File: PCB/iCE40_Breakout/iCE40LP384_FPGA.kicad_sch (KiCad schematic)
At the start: 24 parts, among them J1 Conn_01x08, J2 Conn_01x10, J3 Conn_01x10, Q1 2N7002, SW1 KH-6X6X5H-STM, U1 ICE40LP384-SG32

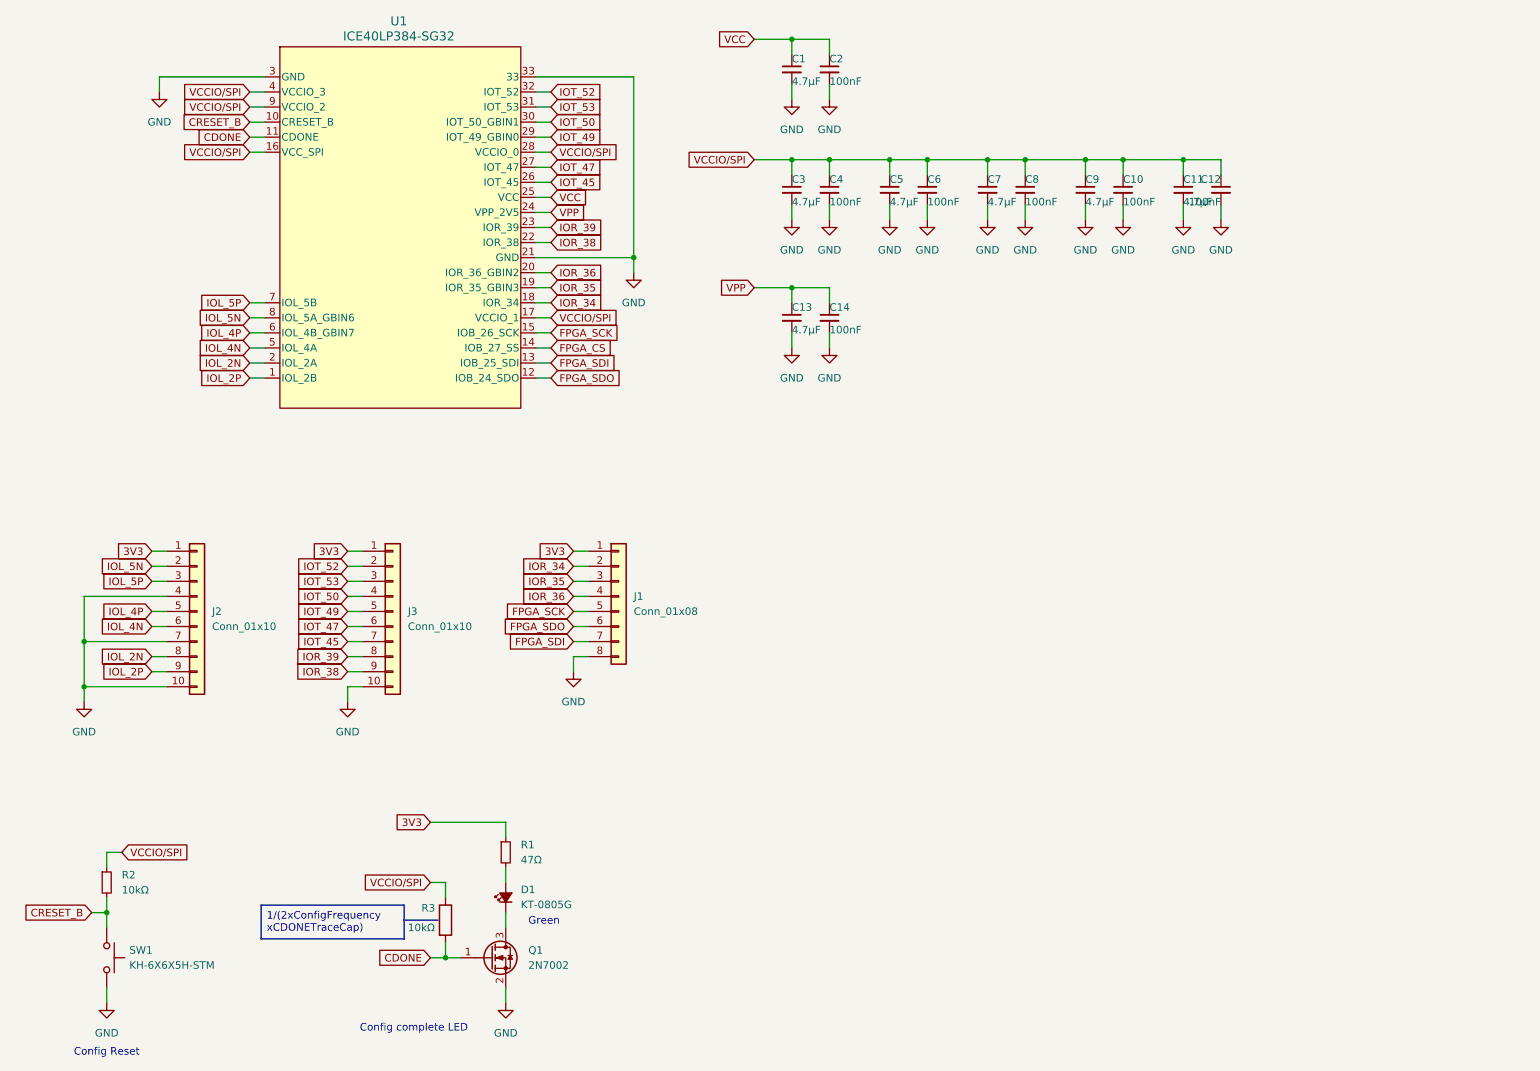
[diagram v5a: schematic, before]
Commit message: Changed all manually placed components into DNP, and changed the manually added caps to 0603
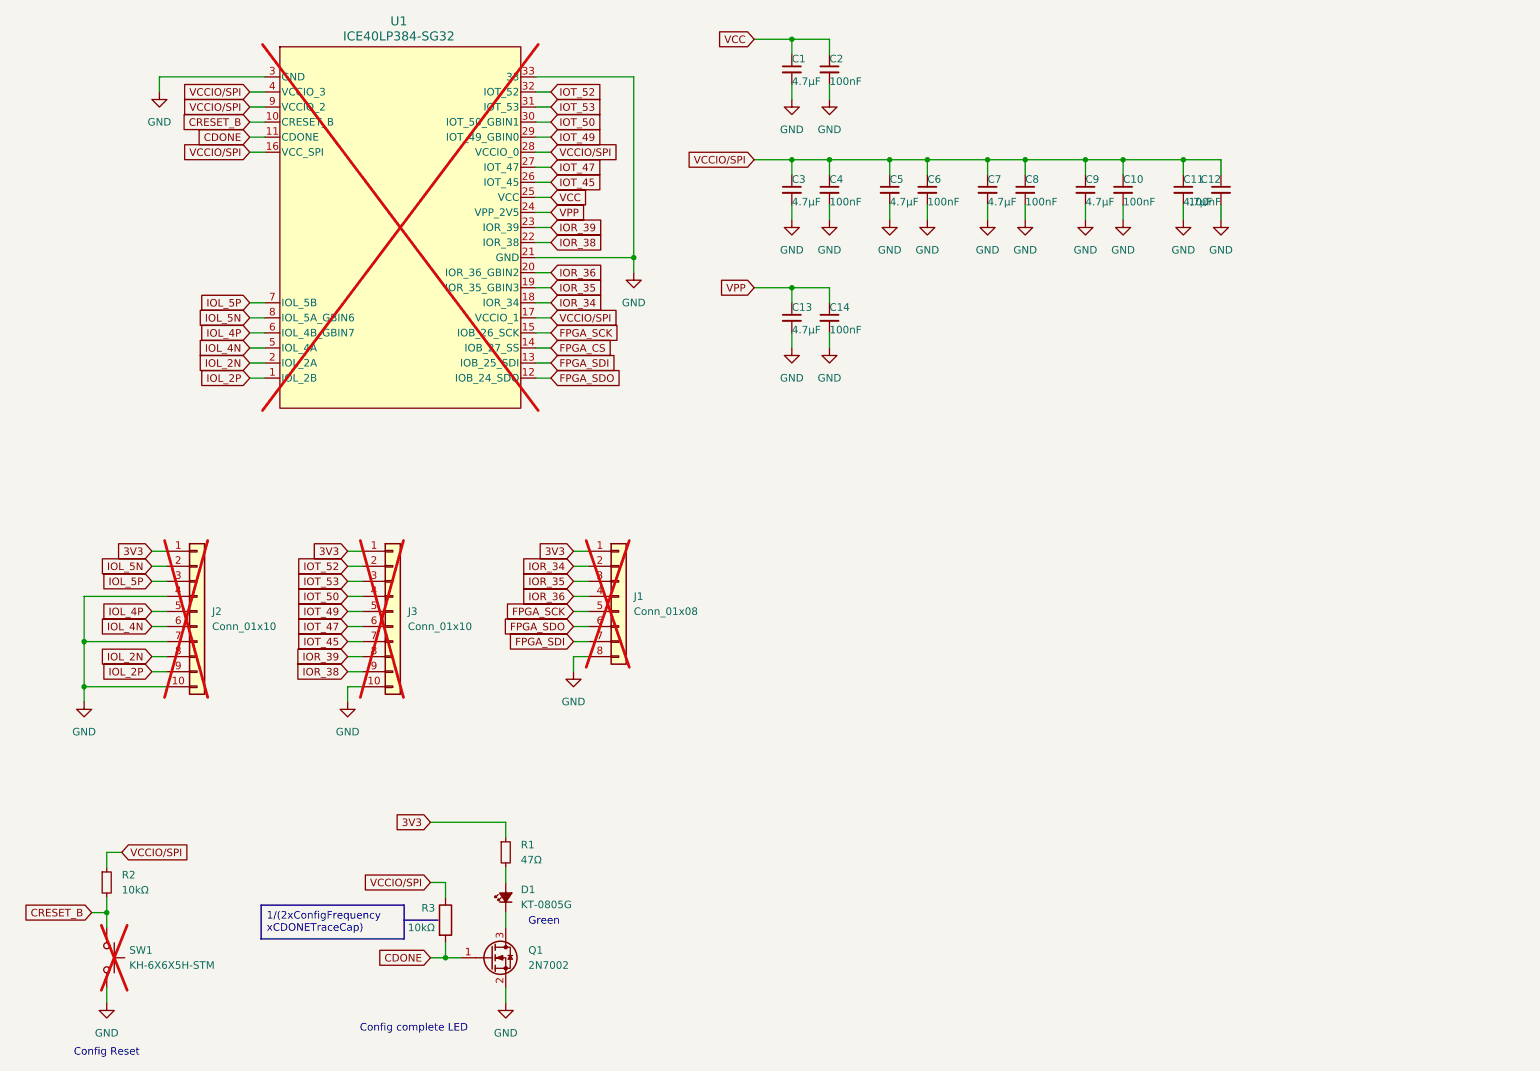
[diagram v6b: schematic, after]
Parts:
- J1, J2, J3, SW1, U1: now not fitted
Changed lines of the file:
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@@
 		(in_bom yes)
 		(on_board yes)
-		(dnp no)
+		(dnp yes)
 		(fields_autoplaced yes)
 		(property "Reference" "J2"
@@
 		(in_bom yes)
 		(on_board yes)
-		(dnp no)
+		(dnp yes)
 		(fields_autoplaced yes)
 		(property "Reference" "SW1"
@@
 		(in_bom yes)
 		(on_board yes)
-		(dnp no)
+		(dnp yes)
 		(fields_autoplaced yes)
 		(property "Reference" "J1"
@@
 		(in_bom yes)
 		(on_board yes)
-		(dnp no)
+		(dnp yes)
 		(fields_autoplaced yes)
 		(property "Reference" "J3"
@@
 		(in_bom yes)
 		(on_board yes)
-		(dnp no)
+		(dnp yes)
 		(property "Reference" "U1"
 			(at 83.566 21.082 0)
